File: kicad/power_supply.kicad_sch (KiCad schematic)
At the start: 0 parts

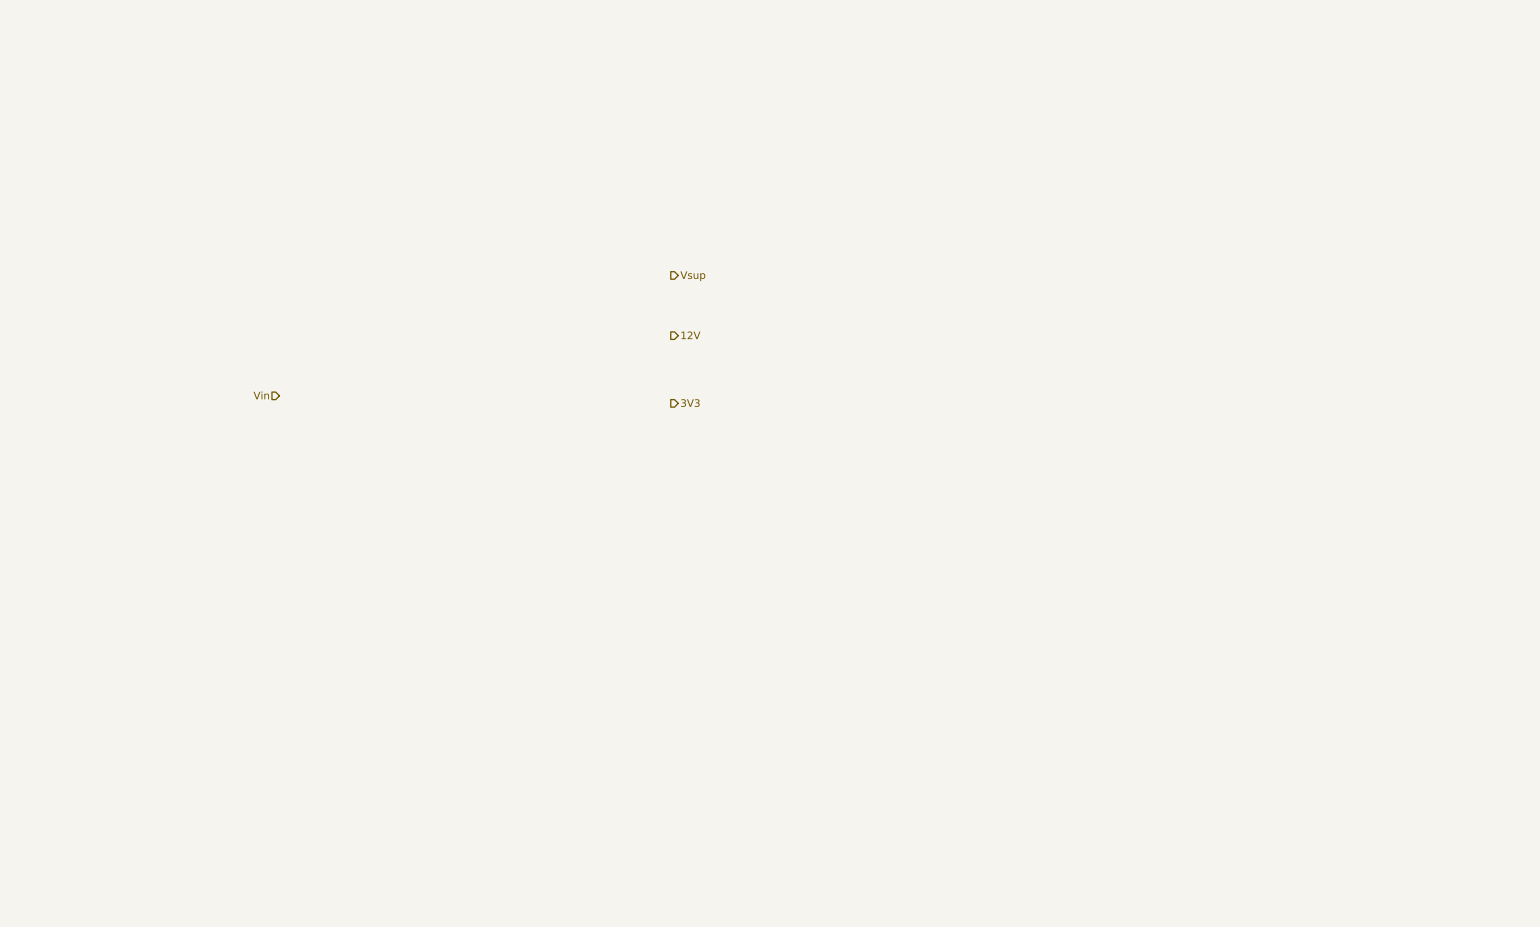
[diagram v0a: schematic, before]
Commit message: Completed the schematic. All components have Digikey part numbers and footprints. The power supply sheet still requires some work.
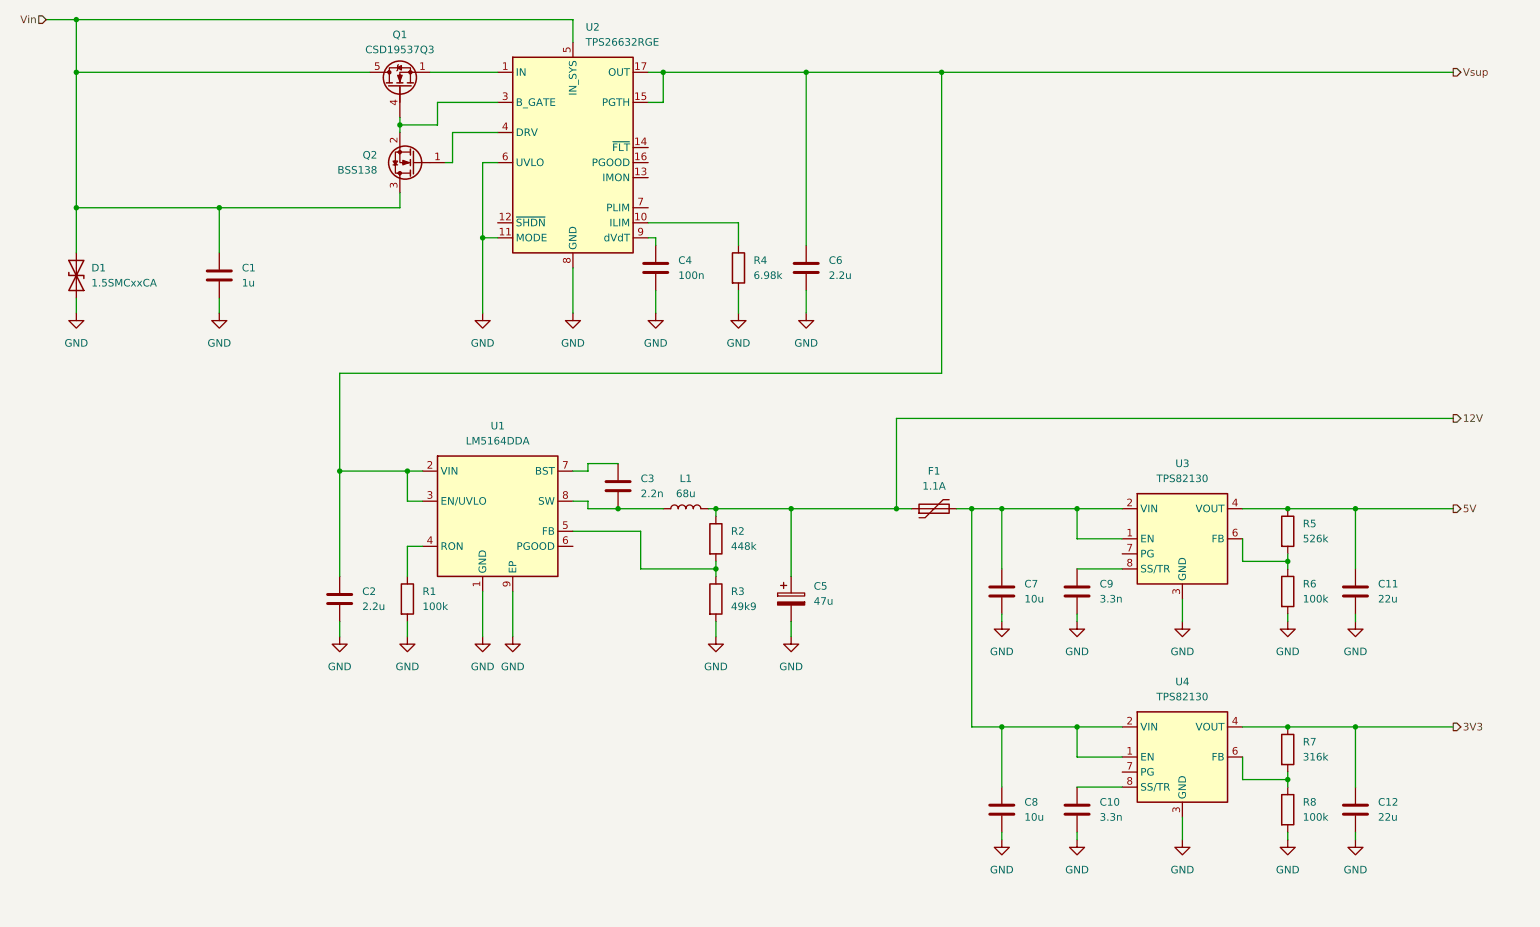
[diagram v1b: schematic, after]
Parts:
- added C1: 1u, Capacitor_SMD:C_0805_2012Metric, symbol Device:C
- added C10, C9: 3.3n, Capacitor_SMD:C_0603_1608Metric, symbol Device:C
- added C11, C12: 22u, Capacitor_SMD:C_Elec_8x6.2, symbol Device:C
- added C2, C6: 2.2u, Capacitor_SMD:C_1206_3216Metric, symbol Device:C
- added C3: 2.2n, Capacitor_SMD:C_0603_1608Metric, symbol Device:C
- added C4: 100n, Capacitor_SMD:C_0603_1608Metric, symbol Device:C
- added C5: 47u, Capacitor_SMD:C_Elec_8x6.2, symbol Device:C_Polarized
- added C7, C8: 10u, Capacitor_SMD:C_1206_3216Metric, symbol Device:C
- added D1: 1.5SMCxxCA, Diode_SMD:D_SMC, symbol Diode:1.5SMCxxCA
- added F1: 1.1A, Fuse:Fuse_2920_7451Metric, symbol Device:Polyfuse
- added L1: 68u, local_library:INDPM102100X400N, symbol Device:L
- added Q1: CSD19537Q3, Package_SON:VSON-8_3.3x3.3mm_P0.65mm_NexFET, symbol Transistor_FET:CSD19537Q3
- added Q2: BSS138, Package_TO_SOT_SMD:SOT-23, symbol Transistor_FET:BSS138
- added R1, R6, R8: 100k, Resistor_SMD:R_0603_1608Metric, symbol Device:R
- added R2: 448k, Resistor_SMD:R_0603_1608Metric, symbol Device:R
- added R3: 49k9, Resistor_SMD:R_0603_1608Metric, symbol Device:R
- added R4: 6.98k, Resistor_SMD:R_0603_1608Metric, symbol Device:R
- added R5: 526k, Resistor_SMD:R_0603_1608Metric, symbol Device:R
- added R7: 316k, Resistor_SMD:R_0603_1608Metric, symbol Device:R
- added U1: LM5164DDA, Package_SO:HSOP-8-1EP_3.9x4.9mm_P1.27mm_EP2.41x3.1mm_ThermalVias, symbol Regulator_Switching:LM5164DDA
- added U2: TPS26632RGE, Package_DFN_QFN:Texas_RGE0024H_VQFN-24-1EP_4x4mm_P0.5mm_EP2.7x2.7mm_ThermalVias, symbol Power_Management:TPS26632RGE
- added U3, U4: TPS82130, Package_LGA:Texas_SIL0008D_MicroSiP-8-1EP_2.8x3mm_P0.65mm_EP1.1x1.9mm_ThermalVias, symbol Regulator_Switching:TPS82130
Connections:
- net 12V: now also C5.1, F1.1, L1.2, R2.1
- net 3V3: now also C12.1, R7.1, U4.4 (VOUT), U4.5 (VOUT)
- net Vin: now also C1.1, D1.2 (A2), Q1.5 (D), Q2.3 (D), U2.5 (IN_SYS)
- net Vsup: now also C2.1, C6.1, U1.2 (VIN), U1.3 (EN/UVLO), U2.15 (PGTH), U2.17 (OUT), U2.18 (OUT)
- new net: R2.2, R3.1, U1.5 (FB)
- new net: C7.1, C8.1, F1.2, U3.1 (EN), U3.2 (VIN), U4.1 (EN), U4.2 (VIN)
- new net: C10.1, U4.8 (SS/TR)
- new net: Q1.1 (S), Q1.2 (S), Q1.3 (S), U2.1 (IN), U2.2 (IN)
- new net: R4.1, U2.10 (ILIM)
- new net: Q1.4 (G), Q2.2 (S), U2.3 (B_GATE)
- new net: Q2.1 (G), U2.4 (DRV)
- new net: C4.1, U2.9 (dVdT)
- new net: R5.2, R6.1, U3.6 (FB)
- new net: C9.1, U3.8 (SS/TR)
- new net: C3.1, U1.7 (BST)
- new net: C3.2, L1.1, U1.8 (SW)
- new net: R7.2, R8.1, U4.6 (FB)
- new net: R1.1, U1.4 (RON)
- new net 5V: C11.1, R5.1, U3.4 (VOUT), U3.5 (VOUT)
- new net GND: C1.2, C10.2, C11.2, C12.2, C2.2, C4.2, C5.2, C6.2, C7.2, C8.2, C9.2, D1.1 (A1), R1.2, R3.2, R4.2, R6.2, R8.2, U1.1 (GND), U1.9 (EP), U2.11 (MODE), U2.25 (GND), U2.6 (UVLO), U2.8 (GND), U3.3 (GND), U3.9 (GND), U4.3 (GND), U4.9 (GND)
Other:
- company: (none) -> NX Solutions
- title: (none) -> TV slider

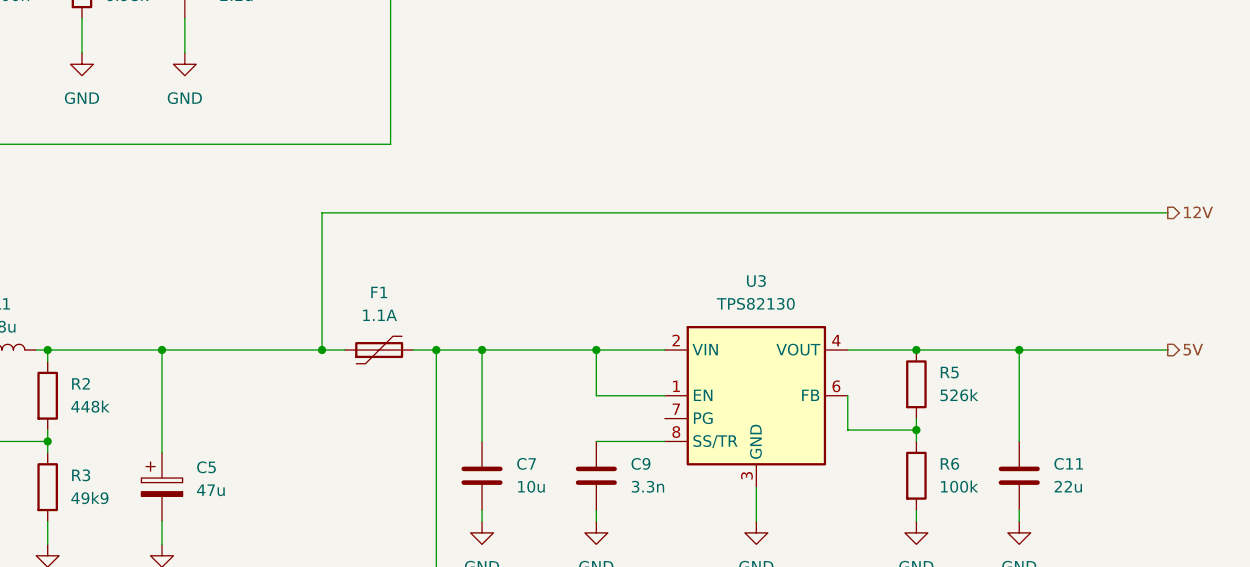
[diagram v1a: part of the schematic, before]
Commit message: Updated footprints and step models. Placed on PCB, but not yet positioned in final location.
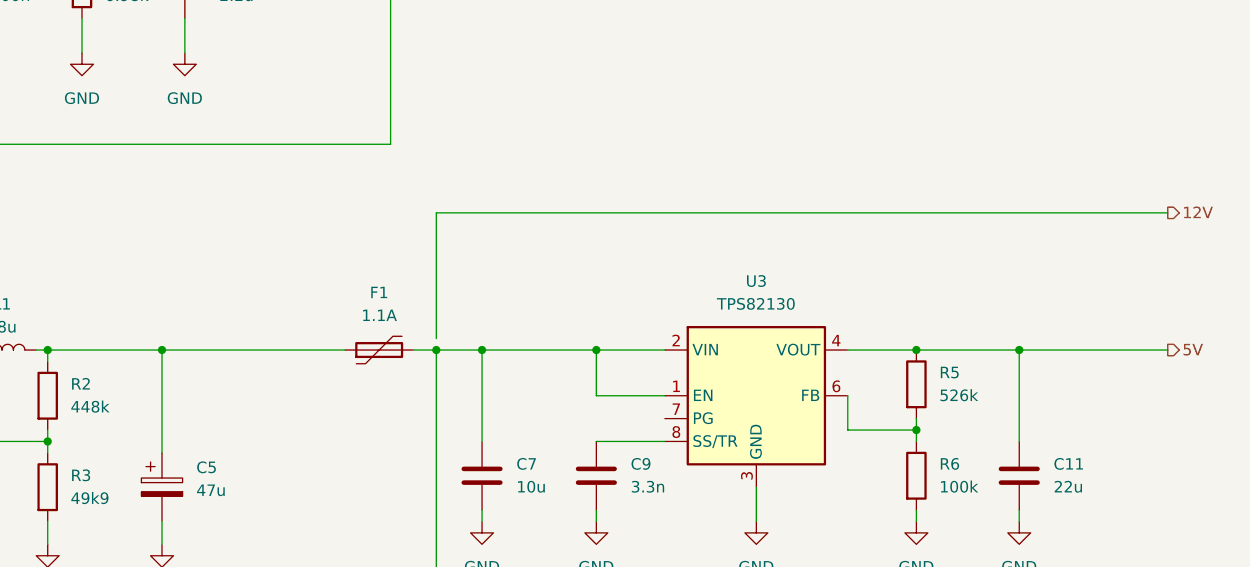
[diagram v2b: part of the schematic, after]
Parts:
- C1: MP GCM21BC72A105KE36L -> GRM21BC72A105KE01L; SupplierPN 490-14436-1-ND -> 490-14464-1-ND
- C10, C9: MP GRM188R71H332KA01D -> GRM188R72A332KA01D; SupplierPN 490-1503-1-ND -> 490-1481-1-ND; Voltage 50V -> 100V
- C11, C12: footprint Capacitor_SMD:C_Elec_8x6.2 -> Capacitor_SMD:C_Elec_6.3x5.8; MF Panasonic -> Kemet; MP EEE-HD1H220P -> A766EB226M1DLAE060; SupplierPN PCE4977CT-ND -> 399-A766EB226M1DLAE060CT-ND; Voltage 50V -> 20V
- C2, C6: Dielectric X7S -> X8L; MP GCM31CC72A225KE02L -> GRM31CL8EL225KE07L; SupplierPN 490-14438-1-ND -> 490-GRM31CL8EL225KE07LCT-ND
- C3: MP GRM188R71H222KA01D -> GRM188R72A222KA01D; SupplierPN 490-1500-1-ND -> 490-1478-1-ND; Voltage 50V -> 100V
- C4: MP GCM188R71H104KA57D -> GRM188R72A104KA35D; SupplierPN 490-4779-1-ND -> 490-3285-1-ND; Voltage 50V -> 100V
- C5: footprint Capacitor_SMD:C_Elec_8x6.2 -> Capacitor_SMD:C_Elec_6.3x5.8; MF Panasonic -> Kemet; MP EEH-ZC1H470P -> A768EB476M1ELAS042; SupplierPN PCE4960CT-ND -> 399-A768EB476M1ELAS042CT-ND; Voltage 50V -> 25V
- C7, C8: footprint Capacitor_SMD:C_1206_3216Metric -> Capacitor_SMD:C_0805_2012Metric; Dielectric X7R -> X5R; MP GRM31CR71E106KA12L -> GRM21BR61E106KA73K; SupplierPN 490-5521-1-ND -> 490-16824-1-ND
- F1: footprint Fuse:Fuse_2920_7451Metric -> local_library:Fuse_2920_7451Metric
- R2, R3, R4, R5, R7: MF YAGEO -> Yageo
- U3, U4: footprint Package_LGA:Texas_SIL0008D_MicroSiP-8-1EP_2.8x3mm_P0.65mm_EP1.1x1.9mm_ThermalVias -> local_library:Texas_SIL0008D_MicroSiP-8-1EP_2.8x3mm_P0.65mm_EP1.1x1.9mm_ThermalVias
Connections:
- net 12V: no longer C5.1, F1.1, L1.2, R2.1
- new net: C5.1, F1.1, L1.2, R2.1

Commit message: Updated all schematic pages except the power supply. Did the initial component placement.
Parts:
- renumbered C4 to C1, C8 to C10, C10 to C11, C6 to C2, C1 to C3, C3 to C4, C7 to C5, C9 to C6, C11 to C7, C2 to C8, C5 to C9, R4 to R1, R5 to R2, R2 to R3, R6 to R4, R1 to R5, R3 to R6, U2 to U1, U1 to U2
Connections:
- net 12V: now also C10.1, C5.1, F1.2, U3.1 (EN), U3.2 (VIN), U4.1 (EN), U4.2 (VIN)

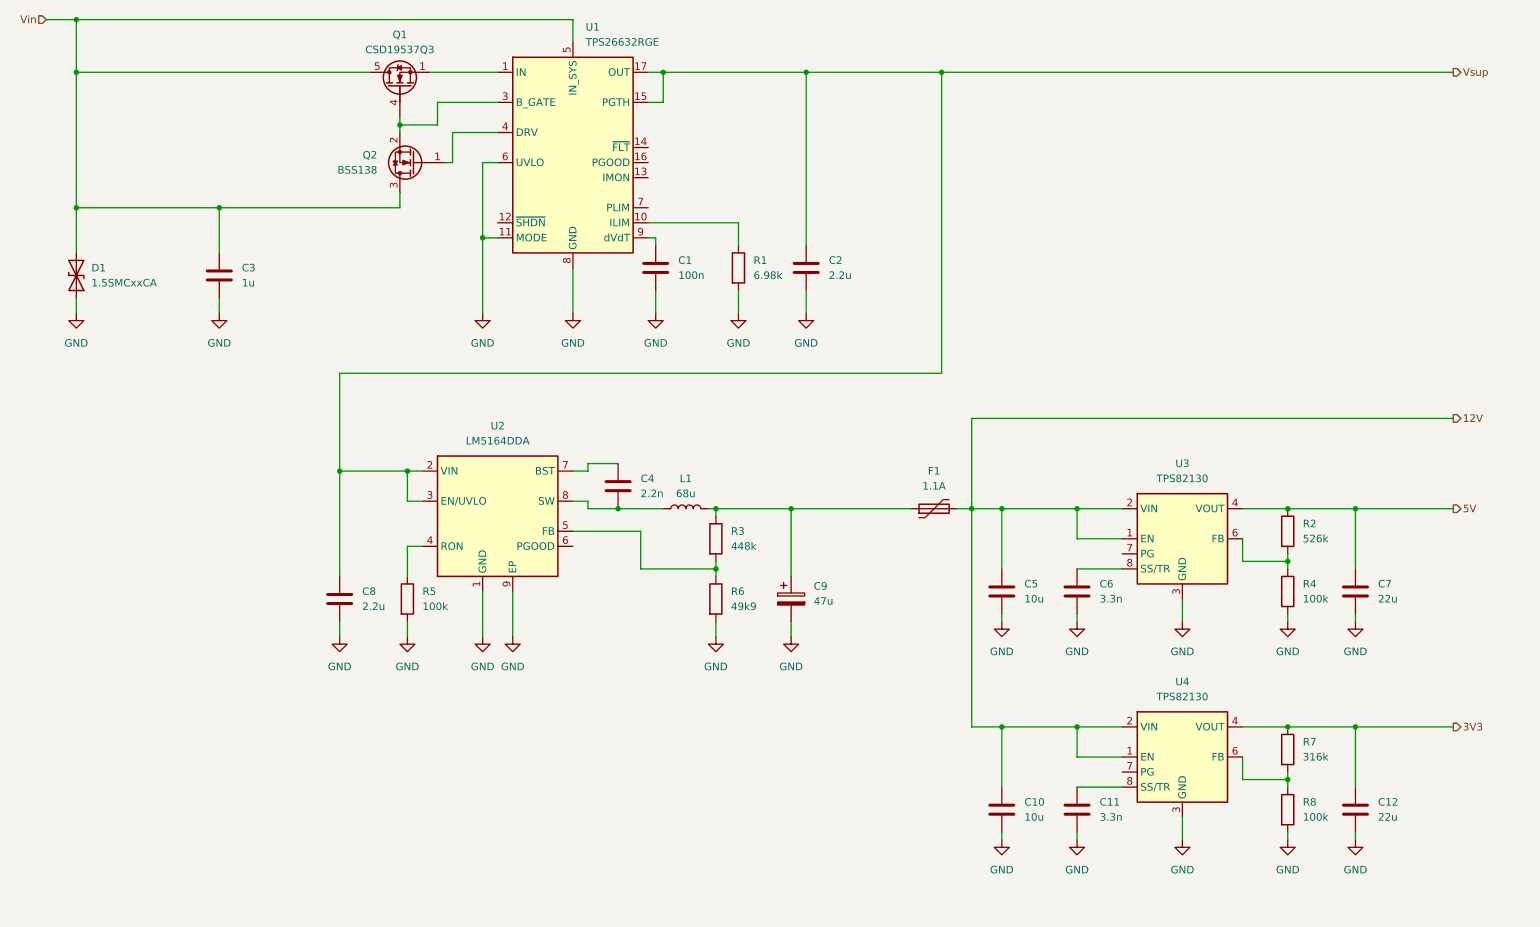
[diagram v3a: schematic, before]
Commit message: Changed power supply chips as the 12V is no longer required.
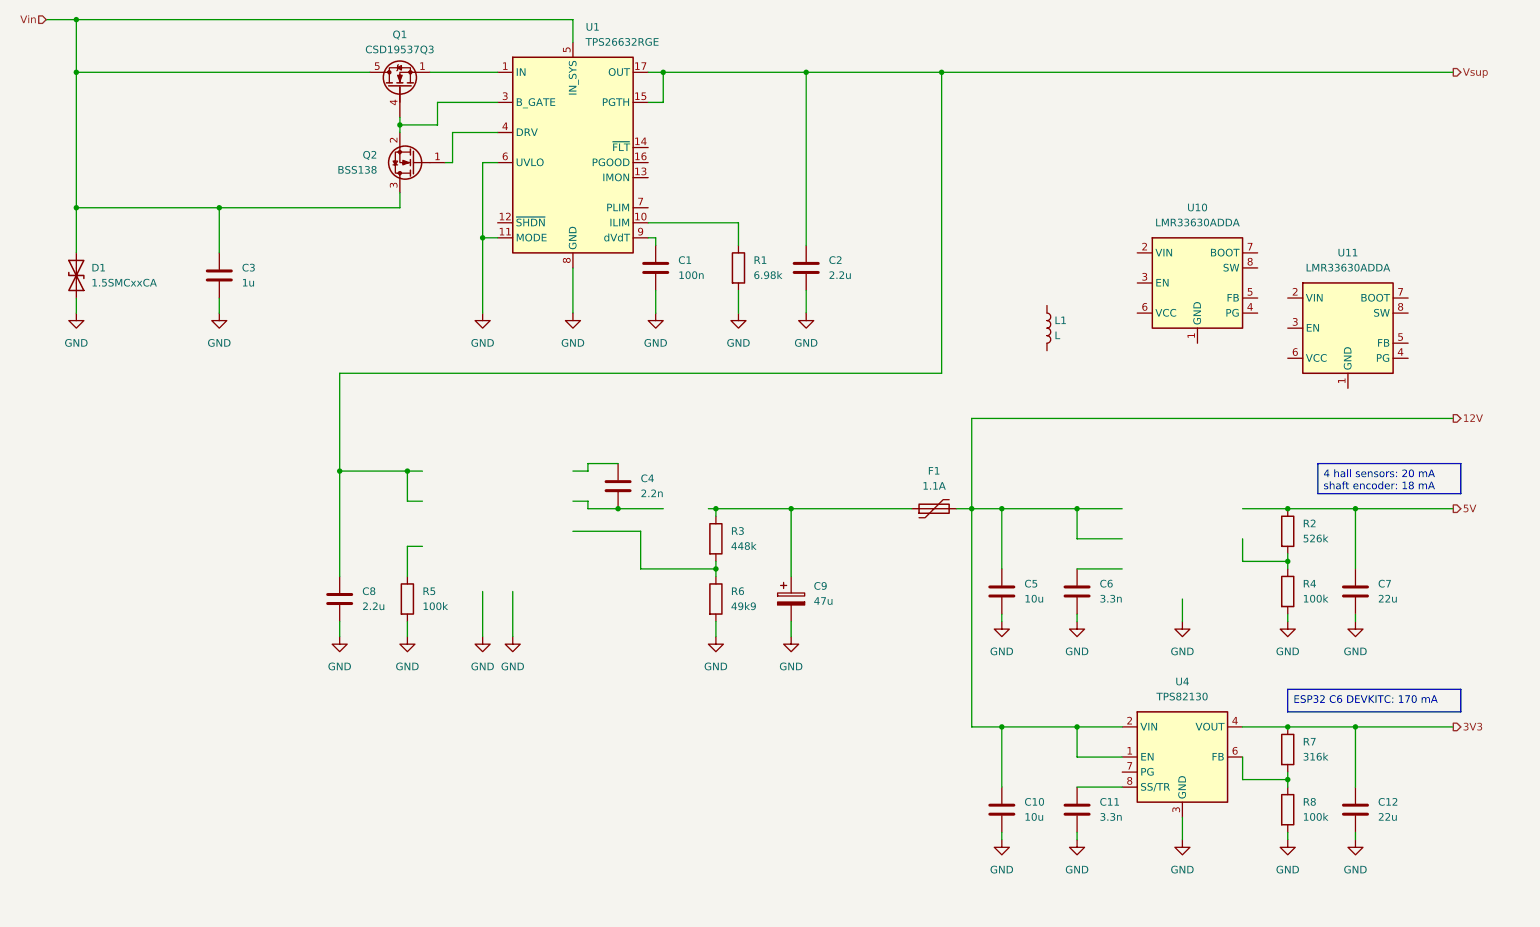
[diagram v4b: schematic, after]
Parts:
- removed U2: LM5164DDA, Package_SO:HSOP-8-1EP_3.9x4.9mm_P1.27mm_EP2.41x3.1mm_ThermalVias, symbol Regulator_Switching:LM5164DDA
- removed U3: TPS82130, local_library:Texas_SIL0008D_MicroSiP-8-1EP_2.8x3mm_P0.65mm_EP1.1x1.9mm_ThermalVias, symbol Regulator_Switching:TPS82130
- added U10, U11: LMR33630ADDA, Package_SO:Texas_HSOP-8-1EP_3.9x4.9mm_P1.27mm_ThermalVias, symbol Regulator_Switching:LMR33630ADDA
- L1: value 68u -> L; footprint local_library:INDPM102100X400N -> (none); MF Coilcraft -> (none); MP MSS1038-683MLC -> (none); Supplier Digi-Key -> (none); SupplierPN 2457-MSS1038-683MLC-ND -> (none)
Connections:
- net at C9.1, F1.1, R3.1: no longer L1.2
- net at L1.1: no longer C4.2
- new net: U11.1 (GND), U11.9 (GND)
- new net: U10.1 (GND), U10.9 (GND)
